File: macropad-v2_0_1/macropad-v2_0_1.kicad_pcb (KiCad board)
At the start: 2 copper layers, 70 x 70 mm, 19 parts, among them J1 Conn_01x04_Male, SW1 Key_1, SW2 Key_2, SW3 Key_3, SW4 Key_4, SW5 Key_5, SW6 Key_6, SW7 Rotary_Encoder_Switch, SW8 Layer_Btn, SW9 Reset_Btn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

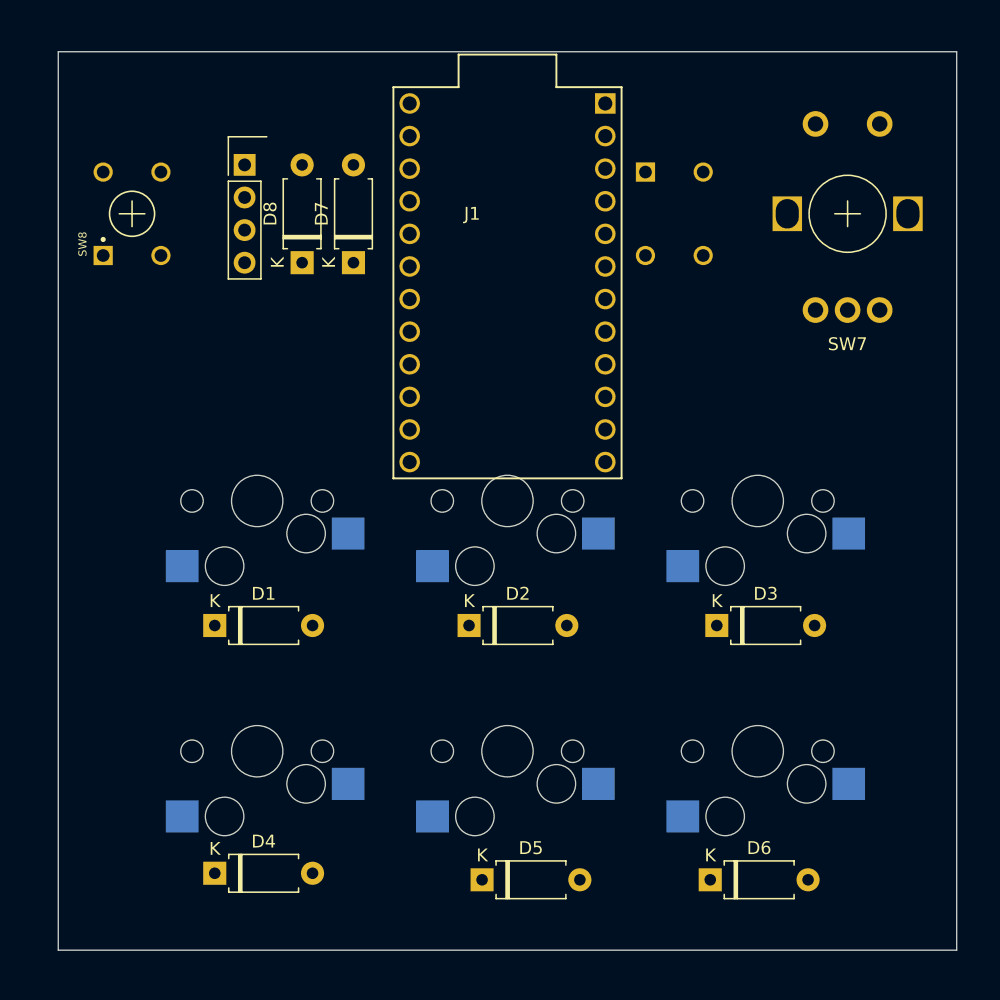
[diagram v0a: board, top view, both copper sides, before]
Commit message: Adding paths to schematic
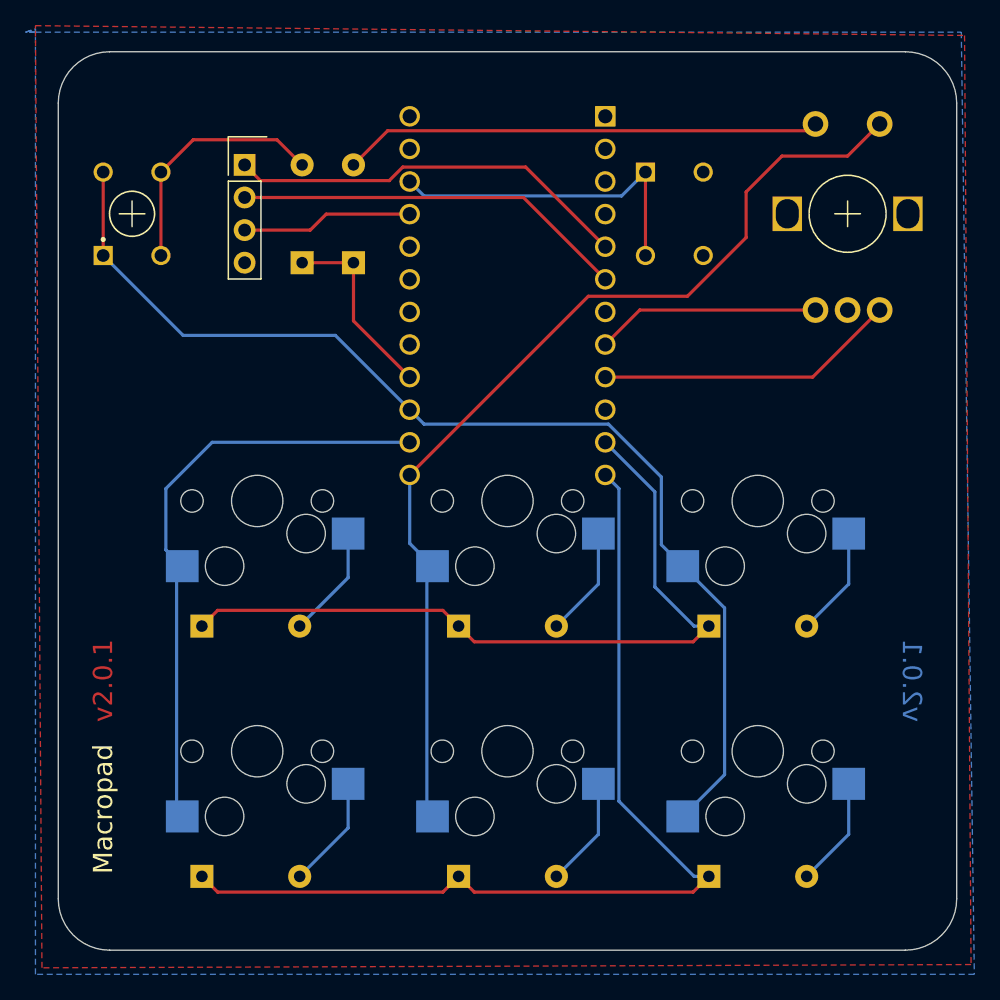
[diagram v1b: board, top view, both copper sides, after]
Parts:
- D1, D2, D3, D4, D5, D6, D7, D8: moved to B.Cu
- moved D5 1.85 mm to (31.2, 64.2)
- moved D4 1.03 mm to (11.2, 64.2)
- moved D1 1.00 mm to (11.2, 44.8)
- moved U1 1.00 mm to (35.0, 19.0)
- moved D2 0.82 mm to (31.2, 44.8)
- moved D3 0.62 mm to (50.7, 44.8)
- moved D6 0.29 mm to (50.7, 64.2)
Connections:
- SW7 pad A: Net-(SW7-PadA) -> Encoder_A
- SW7 pad B: Net-(SW7-PadB) -> Encoder_B
- U1 pad 10: Col_0 -> Net-(U1-Pad10)
- U1 pad 13: Net-(U1-Pad13) -> Col_1
- U1 pad 14: Net-(U1-Pad14) -> Col_0
- U1 pad 15: Net-(SW7-PadA) -> Col_2
- U1 pad 16: Net-(SW7-PadB) -> Row_Extra
- U1 pad 7: Col_2 -> Net-(U1-Pad7)
- U1 pad 8: Col_1 -> Encoder_A
- U1 pad 9: Row_Extra -> Encoder_B
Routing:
- net Col_2: track 0.00 -> 87.0 mm
- net Col_1: track 0.00 -> 77.7 mm
- net Row_1: track 0.00 -> 76.8 mm
- net Row_0: track 0.00 -> 59.9 mm
- net Col_0: track 0.00 -> 47.0 mm
- net Encoder_S1: track 0.00 -> 37.3 mm
- net Net-(J1-Pad1): track 0.00 -> 31.6 mm
- net Net-(J1-Pad2): track 0.00 -> 30.7 mm
- net Net-(SW9-Pad1): track 0.00 -> 26.1 mm
- net Encoder_B: track 0.00 -> 23.5 mm
- net Net-(D8-Pad2): track 0.00 -> 19.4 mm
- net Encoder_A: track 0.00 -> 17.5 mm
- net Row_Extra: track 0.00 -> 14.7 mm
- net VCC: track 0.00 -> 13.4 mm
- net Net-(D4-Pad2): track 0.00 -> 8.77 mm
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- added copper zone on B.Cu, net GND
- added copper zone on F.Cu, net GND
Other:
- outline, holes or cut-outs redrawn
- board text added: "Macropad"
- board text added: "v2.0.1"

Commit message: Adding plots
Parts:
- added Ref**: Val**, Gauntface:gauntface-logo, B.Cu at (8.13, 24.4)
